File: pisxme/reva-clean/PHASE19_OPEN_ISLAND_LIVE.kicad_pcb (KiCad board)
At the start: 6 copper layers, 300 x 180 mm, 76 parts, among them J1 74221-101LF, J2 A70-112-331N126, J3 JAE SM3ZS067U410ABR1000 B-key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, J4 Amphenol 10171746-00021LF USB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, J5 0039300020, J6 0039300020, J7 Raspberry-Pi-5-Compute-Module, Q1 CSD19536KCS, Q2 CSD19536KCS, U1 LM74700QDBVRQ1, U2 LM74700QDBVRQ1, U3 TPSM63606RDLR, U4 TPSM63606RDLR, U5 TPSM63606RDLR, U6 TPD4EUSB30, U7 TUSB9261IPVP, U8 Texas_DRT_3, U9 TPD4EUSB30

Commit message: phase19: record separated M2 storage trial
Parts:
- moved J3 40.0 mm to (290.0, 145.0)
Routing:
- net /STORAGE/SATA_M2_RX_P: track 59.7 -> 30.6 mm
- net /STORAGE/SATA_M2_TX_N: track 57.7 -> 36.4 mm
- net /STORAGE/SATA_M2_RX_N: track 48.5 -> 58.4 mm
- net /STORAGE/SATA_M2_TX_P: track 49.9 -> 51.9 mm

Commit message: phase19: record legal rotated socket trial
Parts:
- removed MECH_M2_2280: JAE SM3ZS067U410ABR1000 / 2280 card envelope, M2_2280_RETENTION_ENVELOPE
- moved C42 35.0 mm to (205.0, 80.0)
- moved C43 35.0 mm to (210.0, 80.0)
- moved R23 35.0 mm to (210.0, 75.0)
- moved Y1 35.0 mm to (205.0, 75.0)
- moved C31 20.0 mm to (225.0, 100.0)
- moved C30 20.0 mm to (225.0, 96.0)
- moved C32 20.0 mm to (225.0, 108.0)
- moved C33 20.0 mm to (225.0, 112.0)
- moved J3 20.0 mm to (270.0, 145.0), turned to 90 degrees
- moved U7 20.0 mm to (240.0, 105.0)
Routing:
- net /STORAGE/SATA_M2_RX_N: track 58.4 -> 114.4 mm
- net /STORAGE/SATA_M2_TX_N: track 36.4 -> 80.8 mm
- net /STORAGE/SATA_M2_RX_P: track 30.6 -> 56.6 mm
- net /STORAGE/BRIDGE_XO: track 61.1 -> 87.0 mm
- net CM5_USB3_TX_P: track 201.5 -> 181.5 mm
- net CM5_USB3_TX_N: track 199.0 -> 179.0 mm
- net CM5_USB3_RX_P: track 196.0 -> 176.0 mm
- net CM5_USB3_RX_N: track 193.5 -> 173.5 mm
- net /STORAGE/BRIDGE_XI: track 48.1 -> 60.4 mm
- net /STORAGE/SATA_M2_TX_P: track 51.9 -> 57.0 mm
- net /STORAGE/BRIDGE_3V3: track 8.66 -> 10.7 mm
- net /STORAGE/BRIDGE_VSSOSC: track 15.2 -> 13.2 mm

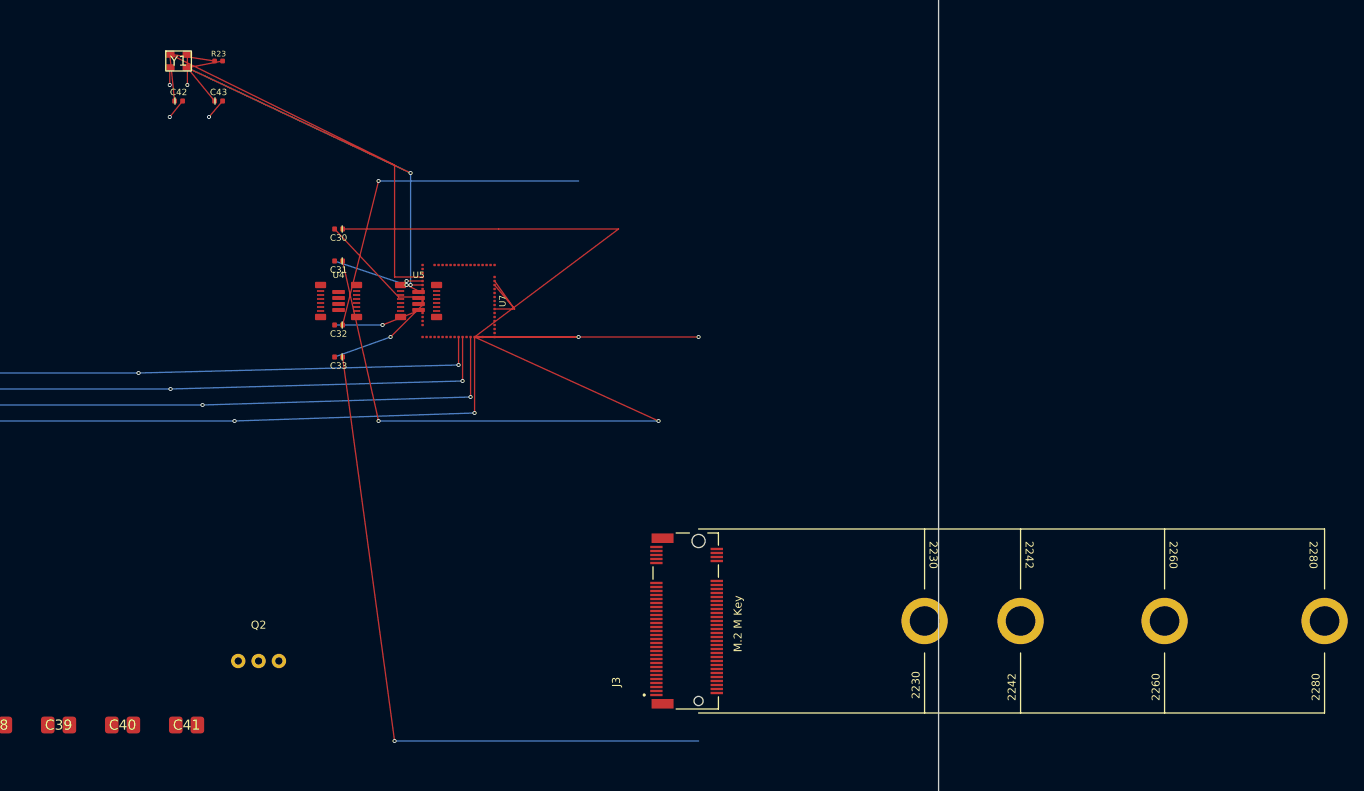
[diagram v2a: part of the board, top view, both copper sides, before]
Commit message: phase19: record opposite-side storage trial
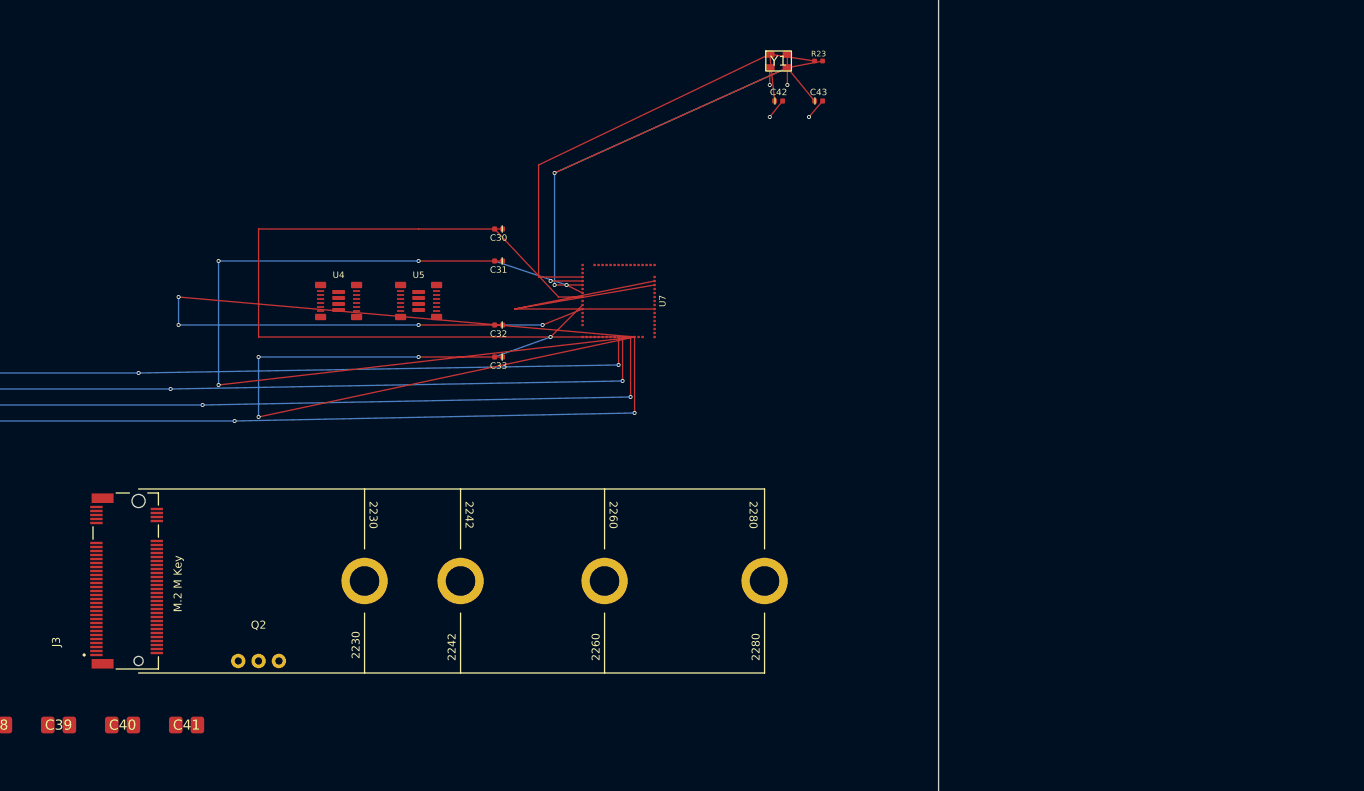
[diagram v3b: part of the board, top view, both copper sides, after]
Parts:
- moved C42 75.0 mm to (280.0, 80.0)
- moved C43 75.0 mm to (285.0, 80.0)
- moved R23 75.0 mm to (285.0, 75.0)
- moved Y1 75.0 mm to (280.0, 75.0)
- moved J3 70.2 mm to (200.0, 140.0)
- moved C30 20.0 mm to (245.0, 96.0)
- moved C31 20.0 mm to (245.0, 100.0)
- moved C32 20.0 mm to (245.0, 108.0)
- moved C33 20.0 mm to (245.0, 112.0)
- moved U7 20.0 mm to (260.0, 105.0)
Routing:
- net /STORAGE/SATA_M2_RX_P: track 56.6 -> 101.2 mm, vias 2 -> 3
- net /STORAGE/BRIDGE_3V3: track 10.7 -> 53.1 mm
- net /STORAGE/SATA_M2_TX_P: track 57.0 -> 91.0 mm
- net /STORAGE/SATA_M2_RX_N: track 114.4 -> 86.1 mm, vias 2 -> 3
- net /STORAGE/SATA_M2_TX_N: track 80.8 -> 103.3 mm, vias 2 -> 3
- net CM5_USB3_RX_N: track 173.5 -> 193.5 mm
- net CM5_USB3_RX_P: track 176.0 -> 196.0 mm
- net CM5_USB3_TX_N: track 179.0 -> 199.0 mm
- net CM5_USB3_TX_P: track 181.5 -> 201.5 mm
- net /STORAGE/BRIDGE_XO: track 87.0 -> 91.2 mm
- net /STORAGE/BRIDGE_XI: track 60.4 -> 63.1 mm
- net /STORAGE/BRIDGE_VSSOSC: track 13.2 -> 15.2 mm

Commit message: phase19: record farther outboard bridge trial
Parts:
- moved C30 20.0 mm to (265.0, 96.0)
- moved C31 20.0 mm to (265.0, 100.0)
- moved C32 20.0 mm to (265.0, 108.0)
- moved C33 20.0 mm to (265.0, 112.0)
- moved U7 20.0 mm to (280.0, 105.0)
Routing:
- net /STORAGE/BRIDGE_3V3: track 53.1 -> 10.7 mm
- net /STORAGE/SATA_M2_TX_P: track 91.0 -> 131.0 mm
- net /STORAGE/SATA_M2_RX_P: track 101.2 -> 141.2 mm
- net /STORAGE/SATA_M2_TX_N: track 103.3 -> 143.2 mm
- net /STORAGE/SATA_M2_RX_N: track 86.1 -> 125.7 mm
- net /STORAGE/BRIDGE_XO: track 91.2 -> 111.2 mm
- net /STORAGE/BRIDGE_XI: track 63.1 -> 83.1 mm
- net /STORAGE/BRIDGE_VSSOSC: track 15.2 -> 35.2 mm
- net CM5_USB3_RX_N: track 193.5 -> 213.5 mm
- net CM5_USB3_RX_P: track 196.0 -> 216.0 mm
- net CM5_USB3_TX_N: track 199.0 -> 219.0 mm
- net CM5_USB3_TX_P: track 201.5 -> 221.5 mm
